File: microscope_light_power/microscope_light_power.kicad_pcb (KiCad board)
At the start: 2 copper layers, 50 x 40 mm, 36 parts, among them J1 MICROUSB, J2 5V175_out, J3 enable_switch, U1 MCP73871-2AA, U2 TPS61090

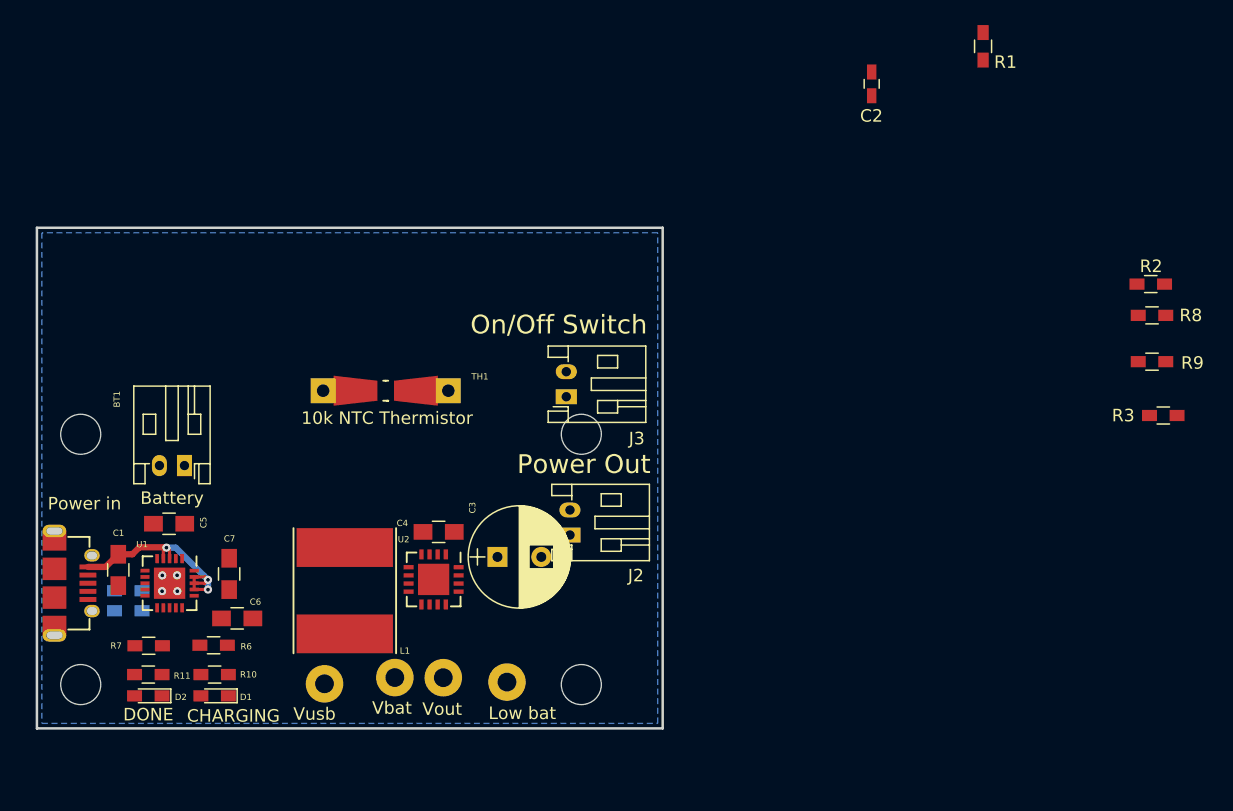
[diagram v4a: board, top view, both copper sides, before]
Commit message: Add resistors to select normally on/normally off output. Scrunch in more components, shift things around a bit, etc etc.
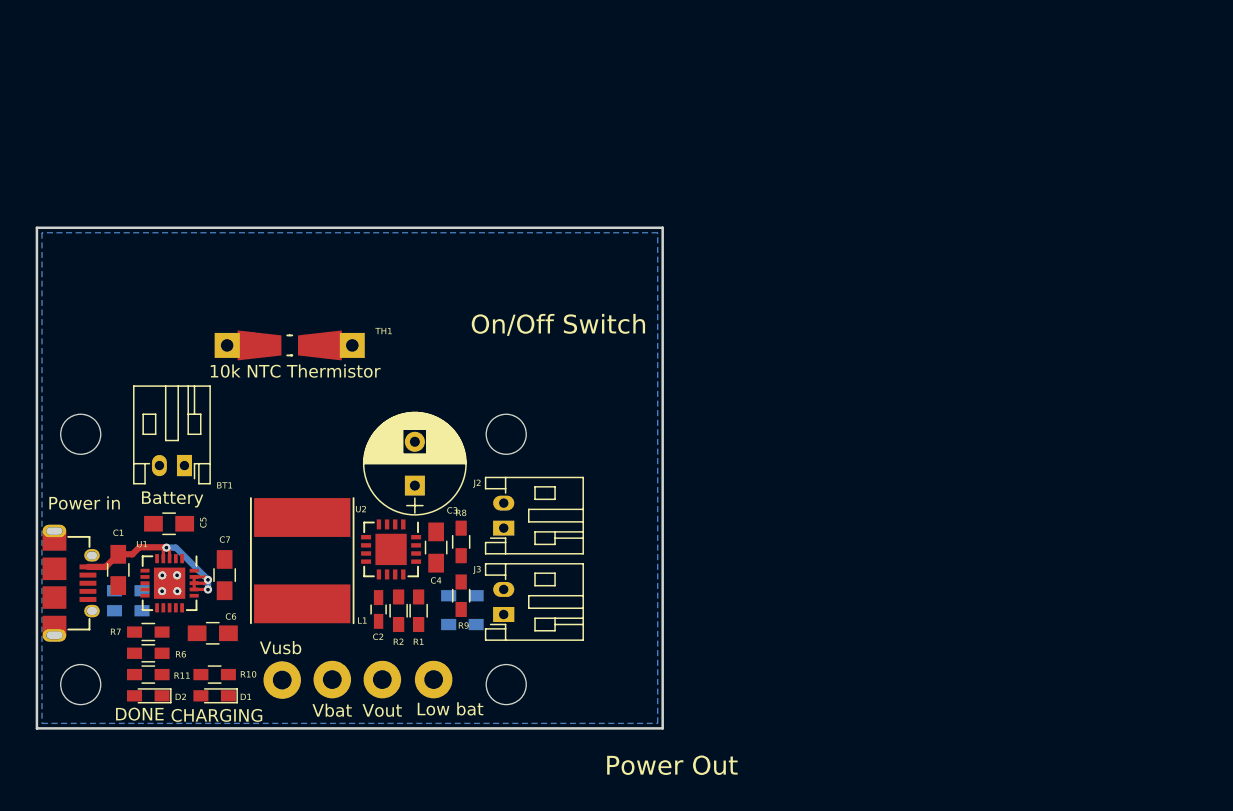
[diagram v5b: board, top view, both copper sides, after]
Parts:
- removed R3: 200k, Resistors_SMD:R_0603_HandSoldering
- added ROff3: 200k, Resistors_SMD:R_0603_HandSoldering, B.Cu at (134.0, 151.7)
- added ROn3: 200k, Resistors_SMD:R_0603_HandSoldering, B.Cu at (134.0, 149.4)
- moved R2 65.5 mm to (128.9, 150.6), turned to 270 degrees
- moved R1 63.8 mm to (130.5, 150.6), turned to 90 degrees
- moved R9 58.3 mm to (133.9, 149.4), turned to 270 degrees
- moved R8 58.1 mm to (133.9, 145.1), turned to 270 degrees
- moved C2 57.6 mm to (127.3, 150.5)
- moved J3 18.1 mm to (137.3, 150.9)
- moved C3 8.72 mm to (130.2, 140.6), turned to 90 degrees
- moved TH1 8.48 mm to (120.2, 129.4)
- moved MK1 6.00 mm to (137.5, 136.5)
- moved MK3 6.00 mm to (137.5, 156.5)
- moved TP2 5.86 mm to (131.7, 156.1)
- moved J2 5.32 mm to (137.3, 144.0)
- moved R6 5.26 mm to (108.9, 154.0)
- moved TP3 5.00 mm to (123.6, 156.1)
- moved TP4 4.87 mm to (127.6, 156.1)
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
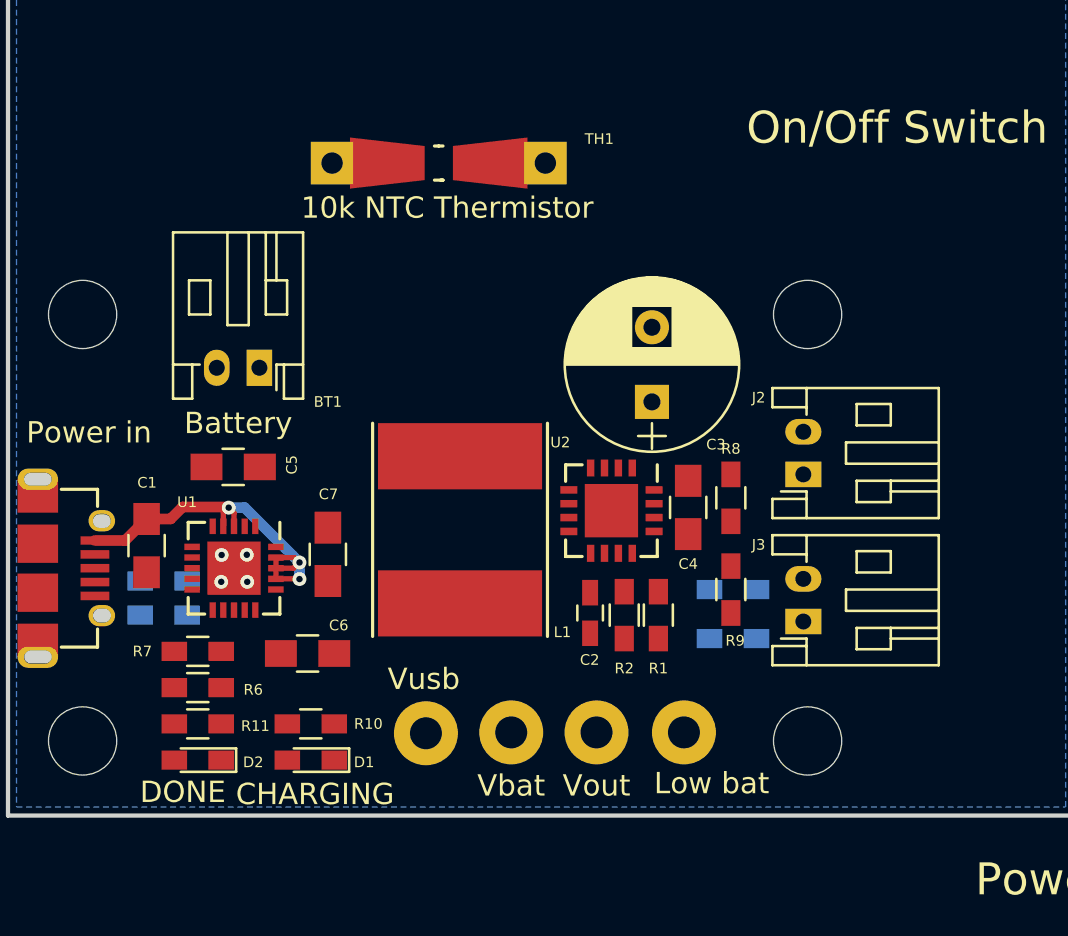
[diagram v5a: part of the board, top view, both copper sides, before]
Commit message: Switch the thermistor footprint to another JST PH connector. Smash everything closer together. Adjusted the test pad footprints.
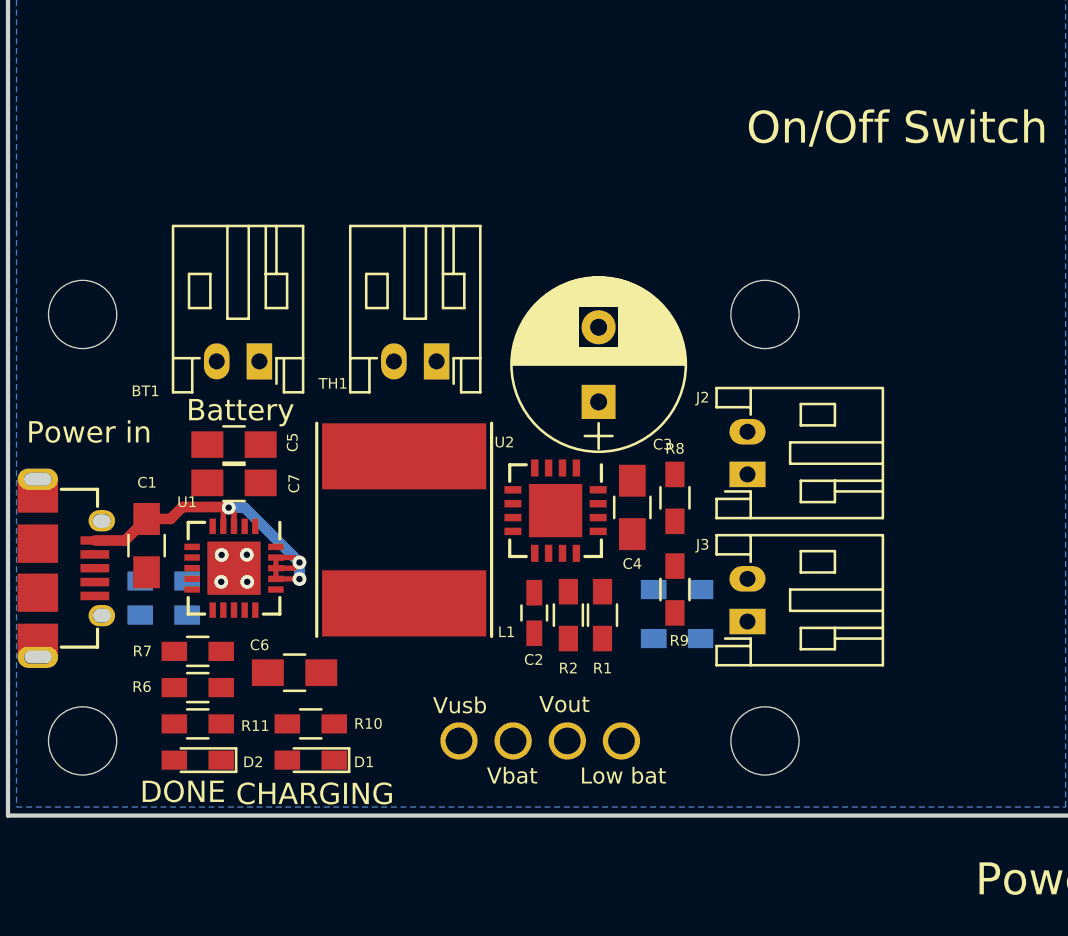
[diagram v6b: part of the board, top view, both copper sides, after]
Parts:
- TH1: footprint Resistors_Universal:Resistor_SMD+THTuniversal_0805to1206_RM10_HandSoldering -> Connectors_JST:JST_PH_S2B-PH-K_02x2.00mm_Angled
- moved TH1 9.30 mm to (120.1, 138.7)
- moved C7 5.53 mm to (110.6, 144.4), turned to 180 degrees
- moved TP2 2.96 mm to (128.8, 156.5)
- moved C4 2.62 mm to (129.3, 145.6)
- moved J2 2.62 mm to (134.7, 144.0)
- moved J3 2.62 mm to (134.7, 150.9)
- moved L1 2.62 mm to (118.6, 146.6)
- moved R1 2.62 mm to (127.9, 150.6)
- moved R2 2.62 mm to (126.3, 150.6)
- moved R8 2.62 mm to (131.3, 145.1)
- moved R9 2.62 mm to (131.3, 149.4)
- moved ROff3 2.62 mm to (131.4, 151.7)
- moved ROn3 2.62 mm to (131.4, 149.4)
- moved U2 2.62 mm to (125.7, 145.7)
- moved C2 2.62 mm to (124.7, 150.5)
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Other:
- board text removed: "10k NTC Thermistor"

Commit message: Route the MCP73871
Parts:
- moved R5 9.09 mm to (105.7, 141.7)
- moved R4 6.02 mm to (105.7, 143.2)
- moved C3 0.71 mm to (127.0, 140.5)
- moved ROff3 0.60 mm to (130.8, 151.6), turned to 180 degrees
- moved ROn3 0.58 mm to (130.8, 149.4)
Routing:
- net /Vusb: track 18.7 -> 57.4 mm, vias 3 -> 4
- net /Vbat: track 0.00 -> 35.1 mm, vias 0 -> 3
- net /Vout: track 0.00 -> 33.1 mm, vias 0 -> 1
- net Net-(TH1-Pad1): track 0.00 -> 20.5 mm, vias 0 -> 2
- net GND: track 0.00 -> 13.2 mm, vias 4 -> 8
- net Net-(R10-Pad2): track 0.00 -> 12.3 mm
- net Net-(R11-Pad2): track 0.00 -> 10.0 mm
- net Net-(R4-Pad1): track 0.00 -> 7.97 mm, vias 0 -> 1
- net Net-(R8-Pad2): track 0.00 -> 6.12 mm
- net /enable: track 0.00 -> 5.11 mm
- net Net-(R6-Pad1): track 0.00 -> 4.16 mm
- net Net-(R7-Pad1): track 0.00 -> 1.98 mm
- net Net-(D2-Pad1): track 0.00 -> 1.70 mm
- net Net-(D1-Pad1): track 0.00 -> 1.70 mm
- added copper zone on F.Cu, net /5V175
- added copper zone on F.Cu, net /SW
- added copper zone on F.Cu, net /Vout
- added copper zone on F.Cu, net GND
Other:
- board size 50 x 40 mm -> 39 x 27 mm
- board text added: "10k NTC Thermistor"
- board text added: "5.175V@1.5A Out"
- board text added: "Jon Neal 2018 https://JonNeal.me https://github.com/microscope_light"
- board text removed: "Power Out"

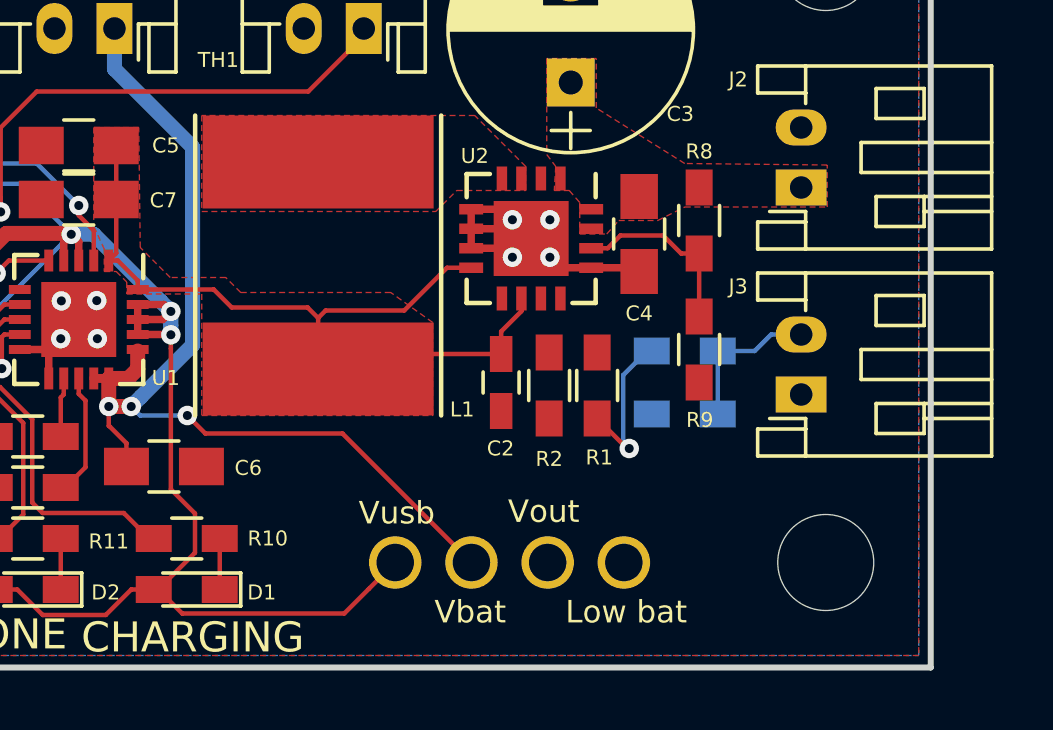
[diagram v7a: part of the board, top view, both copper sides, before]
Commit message: Route TPS61090. Need to add vias and do final adjustment.
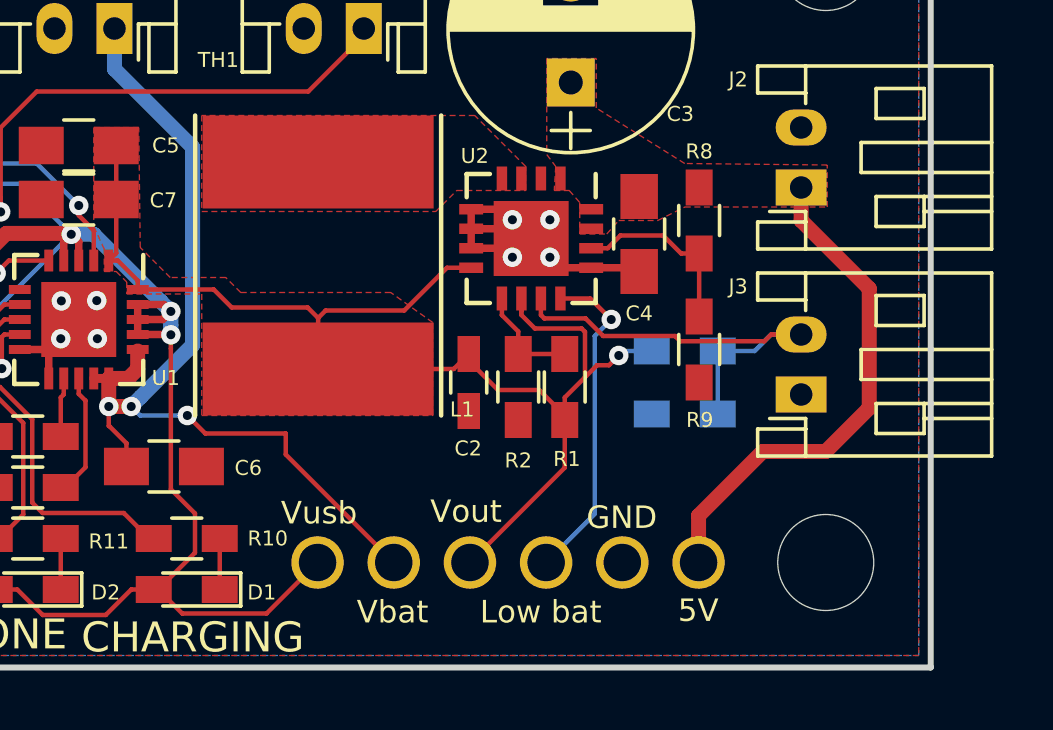
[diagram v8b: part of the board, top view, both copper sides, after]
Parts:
- removed the TP2 at (128.8, 156.5)
- added TP2: TESTPAD, Measurement_Points:Measurement_Point_Round-TH_Big, F.Cu at (131.3, 156.5)
- added TP2: TESTPAD, Measurement_Points:Measurement_Point_Round-TH_Big, F.Cu at (128.7, 156.5)
- added TP2: TESTPAD, Measurement_Points:Measurement_Point_Round-TH_Big, F.Cu at (126.2, 156.5)
- moved TP1 2.59 mm to (118.6, 156.5)
- moved TP3 2.59 mm to (121.1, 156.5)
- moved TP4 2.59 mm to (123.6, 156.5)
- moved R1 1.08 mm to (126.8, 150.7)
- moved C2 1.08 mm to (123.6, 150.5)
- moved R2 1.03 mm to (125.2, 150.7)
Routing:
- net /5V175: track 0.00 -> 17.0 mm
- net /Vout: track 33.1 -> 45.0 mm
- net /low_battery: track 0.00 -> 11.0 mm, vias 0 -> 1
- net /enable: track 5.11 -> 14.8 mm
- net Net-(R1-Pad2): track 0.00 -> 3.63 mm
- net /Vusb: track 57.4 -> 54.8 mm
- net /Vbat: track 35.1 -> 32.9 mm
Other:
- board text added: "5V"
- board text added: "GND"
